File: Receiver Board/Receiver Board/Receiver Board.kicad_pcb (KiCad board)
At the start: 2 copper layers, 31 parts, among them J1 Input Wires, J2 CAN Termination, J3 USB_B_Micro, J4 ICSP Header, J5 Additional Output, J6 Signal Rail, J7 PWR Rail, J8 GND Rail, SW1 RESET BTN, U1 TJA1050, U2 MCP2515T-I_SO(SOIC18), U3 ATMEGA32U4-AU, Y1 8MHz Crystal, Y2 Crystal

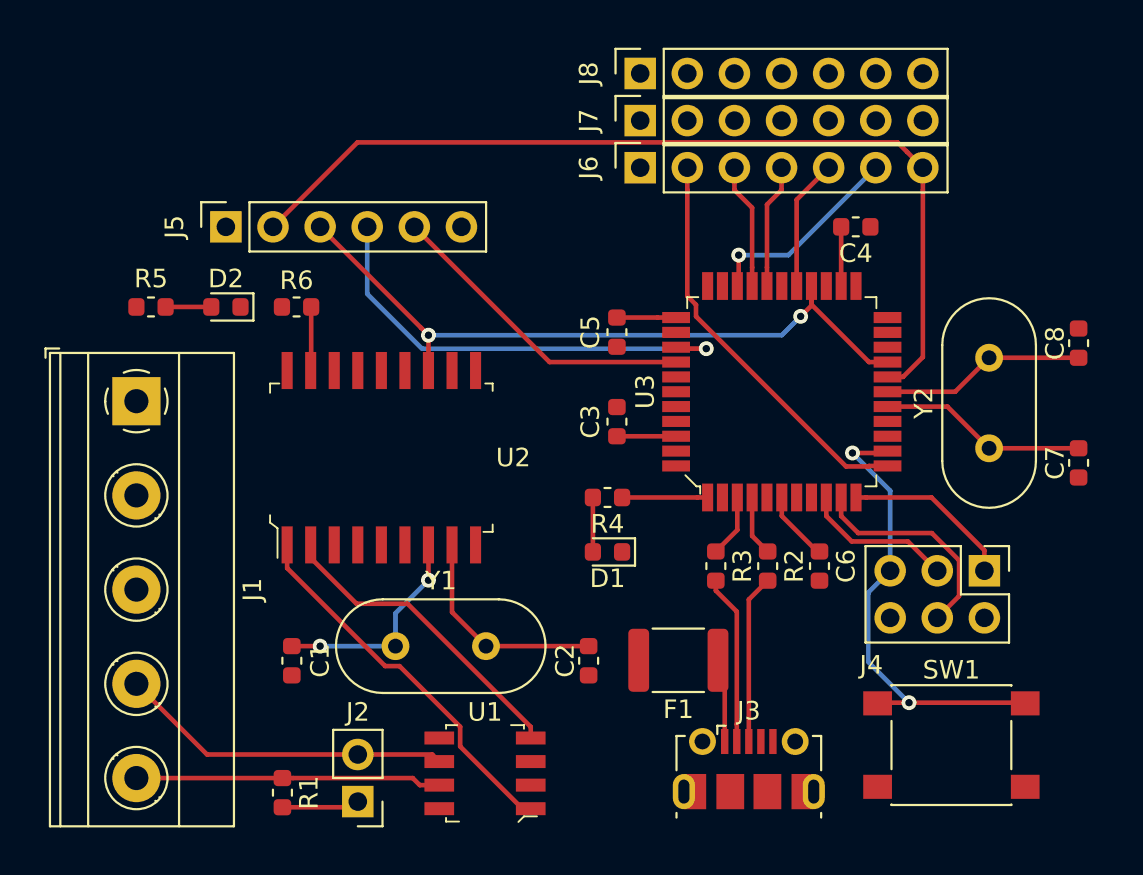
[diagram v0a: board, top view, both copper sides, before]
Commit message: Board layout done, need to update 3d models
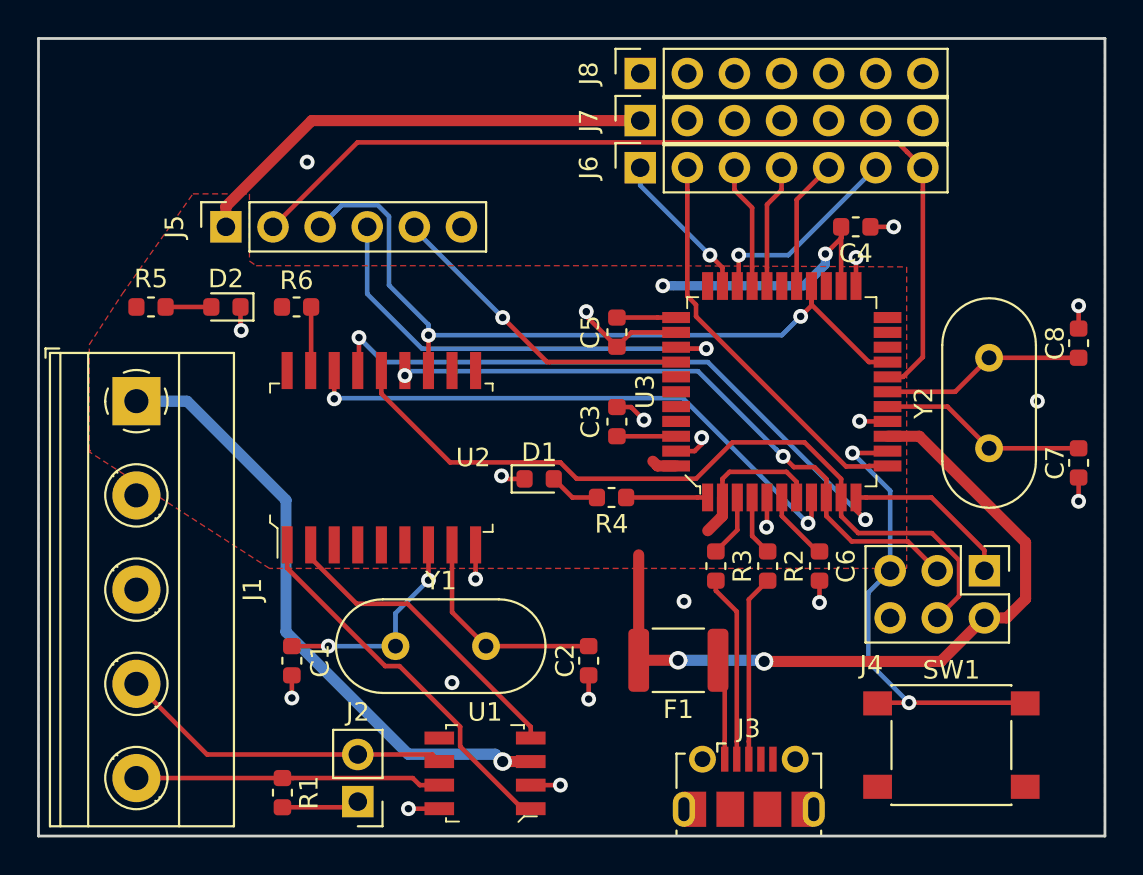
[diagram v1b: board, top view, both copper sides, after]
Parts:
- moved D1 5.39 mm to (150.5, 55.2), turned to 0 degrees
- moved J3 0.95 mm to (161.8, 71.8)
- moved R4 0.22 mm to (154.4, 56.2)
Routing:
- net +5V: track 6.38 -> 127.4 mm, vias 0 -> 5
- net /MISO: track 9.20 -> 43.8 mm, vias 0 -> 2
- net /~CS: track 0.00 -> 31.4 mm, vias 0 -> 2
- net /MOSI: track 11.9 -> 42.5 mm
- net GND: track 0.00 -> 29.6 mm, vias 0 -> 21
- net /SCK: track 8.20 -> 34.4 mm, vias 0 -> 2
- net /CH7: track 0.00 -> 8.22 mm, vias 0 -> 1
- net /~INT: track 38.9 -> 42.4 mm
- net Net-(J3-Pad3): track 9.09 -> 10.0 mm
- net Net-(J3-Pad2): track 9.14 -> 10.1 mm
- net Net-(F1-Pad1): track 4.53 -> 5.48 mm
- net /A1: track 17.1 -> 17.2 mm, vias 0 -> 1
- added copper zone on F.Cu, net +5V
- added copper zone on B.Cu, net GND
- added copper zone on F.Cu, net GND
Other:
- board outline added: 57.5 x 43 mm

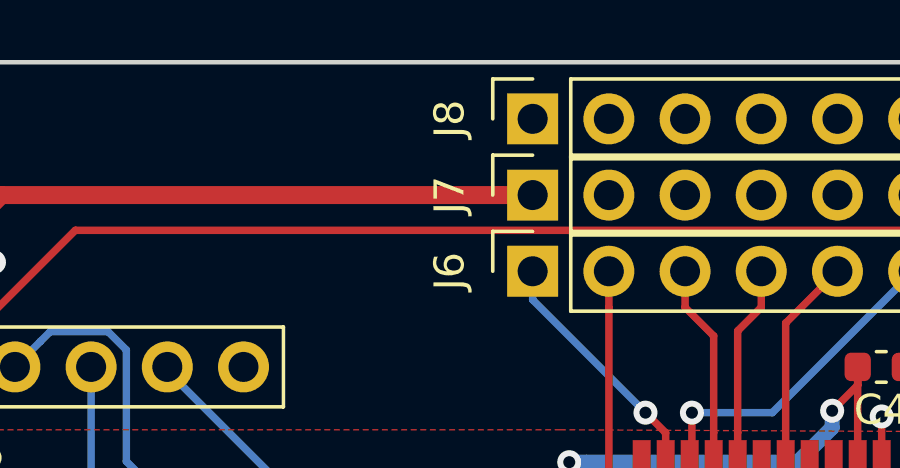
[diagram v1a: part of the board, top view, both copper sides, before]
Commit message: Finished Receiver Board
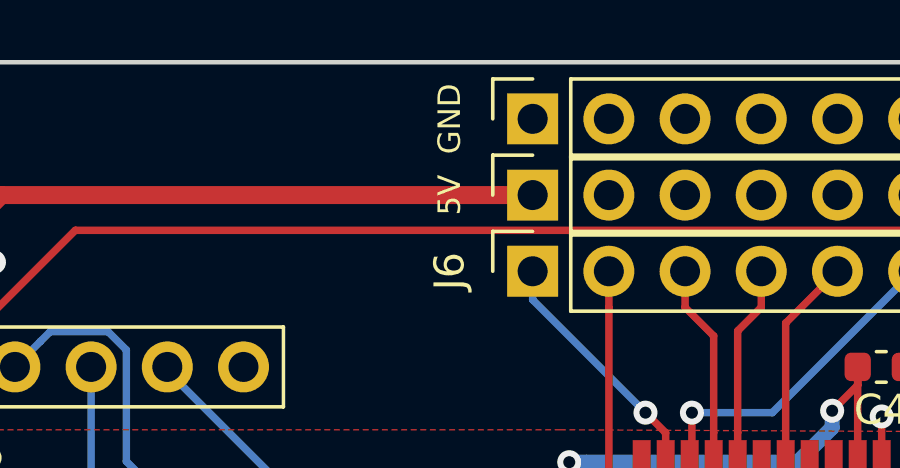
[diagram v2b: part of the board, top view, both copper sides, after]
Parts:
- renumbered J7 to 5V, J8 to GND
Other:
- board text added: "+12V"
- board text added: "+5V"
- board text added: "CANH"
- board text added: "CANL"
- board text added: "GND"
- board text added: "Receiver Board Version 1.0 UW Sailbot By: Andrew Xu"
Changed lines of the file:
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@@
   (general
     (thickness 1.6)
-    (drawings 4)
+    (drawings 10)
     (tracks 288)
     (zones 0)
@@
       (outputformat 1)
       (mirror false)
-      (drillshape 1)
+      (drillshape 0)
       (scaleselection 1)
-      (outputdirectory ""))
+      (outputdirectory "../Receiver Board Gerbers/"))
   )
   (net 0 "")
@@
     (pad 2 smd roundrect (at 2.1375 0 180) (size 1.125 3.4) (layers F.Cu F.Paste F.Mask) (roundrect_rratio 0.222222)
       (net 2 +5V))
+    (model "C:/Users/andre/Documents/GitHub/electrical_board_designs_2018/3D Models/mf-msmf050.stp"
+      (at (xyz 0 0 0))
+      (scale (xyz 1 1 1))
+      (rotate (xyz 90 0 90))
+    )
   )
   (module TerminalBlock_Phoenix:TerminalBlock_Phoenix_MKDS-1,5-5-5.08_1x05_P5.08mm_Horizontal (layer F.Cu)
@@
     (pad 5 thru_hole circle (at 20.32 0 270) (size 2.6 2.6) (drill 1.3) (layers *.Cu *.Mask)
       (net 5 /CANH))
-    (model ${KISYS3DMOD}/TerminalBlock_Phoenix.3dshapes/TerminalBlock_Phoenix_MKDS-1,5-5-5.08_1x05_P5.08mm_Horizontal.wrl
-      (at (xyz 0 0 0))
+    (model C:/Users/andre/Documents/GitHub/electrical_board_designs_2018/TerminalBlock_Phoenix.3dshapes/TerminalBlock_Phoenix_MKDS1.5-5pol.wrl
+      (offset (xyz 10 0 0))
       (scale (xyz 1 1 1))
       (rotate (xyz 0 0 0))
@@
     (pad 6 smd rect (at -2.9 1.2375) (size 1.2 1.9) (layers F.Cu F.Mask)
       (net 4 GND))
-    (model ${KISYS3DMOD}/Connector_USB.3dshapes/USB_Micro-B_Molex-105017-0001.wrl
+    (model ${KISYS3DMOD}/Connector_USB.3dshapes/USB_Micro-B_Molex_47346-0001.step
       (at (xyz 0 0 0))
       (scale (xyz 1 1 1))
@@
     (descr "Through hole straight socket strip, 1x07, 2.54mm pitch, single row (from Kicad 4.0.7), script generated")
     (tags "Through hole socket strip THT 1x07 2.54mm single row")
-    (fp_text reference J7 (at 0 -2.77 90) (layer F.SilkS)
-      (effects (font (size 1 1) (thickness 0.15)))
+    (fp_text reference 5V (at 0 -2.77 90) (layer F.SilkS)
+      (effects (font (size 0.75 0.75) (thickness 0.15)))
     )
     (fp_text value "PWR Rail" (at 0 18.01 90) (layer F.Fab)
@@
     (descr "Through hole straight socket strip, 1x07, 2.54mm pitch, single row (from Kicad 4.0.7), script generated")
     (tags "Through hole socket strip THT 1x07 2.54mm single row")
-    (fp_text reference J8 (at 0 -2.77 90) (layer F.SilkS)
-      (effects (font (size 1 1) (thickness 0.15)))
+    (fp_text reference GND (at 0 -2.77 90) (layer F.SilkS)
+      (effects (font (size 0.75 0.75) (thickness 0.15)))
     )
     (fp_text value "GND Rail" (at 0 18.01 90) (layer F.Fab)
@@
     )
   )
+  (gr_text CANH (at 125.1585 71.374 270) (layer B.SilkS)
+    (effects (font (size 1 1) (thickness 0.25)) (justify mirror))
+  )
+  (gr_text CANL (at 125.1585 66.294 270) (layer B.SilkS)
+    (effects (font (size 1 1) (thickness 0.25)) (justify mirror))
+  )
+  (gr_text GND (at 125.1585 61.214 270) (layer B.SilkS)
+    (effects (font (size 1 1) (thickness 0.25)) (justify mirror))
+  )
+  (gr_text +12V (at 125.1585 56.134 270) (layer B.SilkS)
+    (effects (font (size 1 1) (thickness 0.25)) (justify mirror))
+  )
+  (gr_text +5V (at 125.1585 51.054 270) (layer B.SilkS)
+    (effects (font (size 1 1) (thickness 0.25)) (justify mirror))
+  )
+  (gr_text "Receiver Board\nVersion 1.0\nUW Sailbot\nBy: Andrew Xu" (at 173.2915 51.3715) (layer B.SilkS)
+    (effects (font (size 1.5 1.5) (thickness 0.3)) (justify left mirror))
+  )
   (gr_line (start 123.5 31.5) (end 123.5 74.5) (layer Edge.Cuts) (width 0.15))
